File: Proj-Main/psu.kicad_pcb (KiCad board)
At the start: 2 copper layers, 100 x 75 mm, 129 parts, among them J1 T1A, J2 T1B, J3 T1C, J4 OUT+, J5 SENSE, J6 METER, J7 OUT-, Q1 BC856, Q10 PMP4201Y, Q11 MMBT3904, Q12 PMP4201Y, Q13 BC856, Q14 MMBT2907A, Q15 BC856, Q16 MMBT3904, Q17 BC856, Q18 MMBT3904, Q19 MMBT2907A, Q2 MMBT3904, Q20 MMBT3904, Q21 TIP105, Q22 PZT2222A, Q23 PMP4201Y, Q24 MMBT2907A, Q3 PZT2222A, Q4 BC856, Q5 PMP4201Y, Q6 MMBT3906, Q7 MMBT3906, Q8 PMP4201Y, Q9 MMBT3904

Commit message: PCB tweaks
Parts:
- moved Q2 7.00 mm to (138.0, 116.0), turned to 90 degrees
- moved R3 6.58 mm to (138.0, 122.0), turned to 180 degrees
- moved RV2 6.37 mm to (146.2, 103.2), turned to 0 degrees
- moved R2 5.32 mm to (138.0, 119.5), turned to 0 degrees
- moved R10 4.59 mm to (137.2, 105.0), turned to 270 degrees
- moved C10 4.53 mm to (164.0, 124.0)
- moved R48 4.53 mm to (167.0, 124.0)
- moved DZ1 4.51 mm to (141.5, 105.2)
- moved C1 4.50 mm to (133.5, 117.0)
- moved R1 4.50 mm to (133.5, 119.5)
- moved R4 4.50 mm to (133.5, 114.5)
- moved D9 3.78 mm to (141.5, 101.2), turned to 270 degrees
- moved C7 2.80 mm to (141.5, 94.8), turned to 0 degrees
- moved R15 1.52 mm to (141.0, 92.2), turned to 0 degrees
- moved TP4 1.41 mm to (137.5, 101.0)
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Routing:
- net CGND: track 428.0 -> 440.2 mm, vias 29 -> 28
- net Net-(C7-Pad2): track 18.2 -> 8.43 mm
- net Net-(DZ1-Pad1): track 29.2 -> 20.8 mm
- net GND: track 365.0 -> 372.4 mm, vias 22 -> 21
- net V-UNREG: track 243.2 -> 249.4 mm
- net Net-(Q1-Pad1): track 11.0 -> 4.86 mm
- net -12: track 279.4 -> 285.5 mm
- net Net-(RV1-Pad3): track 2.53 -> 8.54 mm
- net /OUT-: track 138.2 -> 132.4 mm
- net Net-(C1-Pad1): track 10.9 -> 5.58 mm
- net Net-(C1-Pad2): track 17.2 -> 12.0 mm
- net Net-(Q2-Pad1): track 7.07 -> 12.2 mm
- net Net-(C6-Pad2): track 5.20 -> 8.74 mm
- net +2: track 273.9 -> 271.1 mm, vias 10 -> 9
- net Net-(C11-Pad2): track 62.6 -> 60.0 mm
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
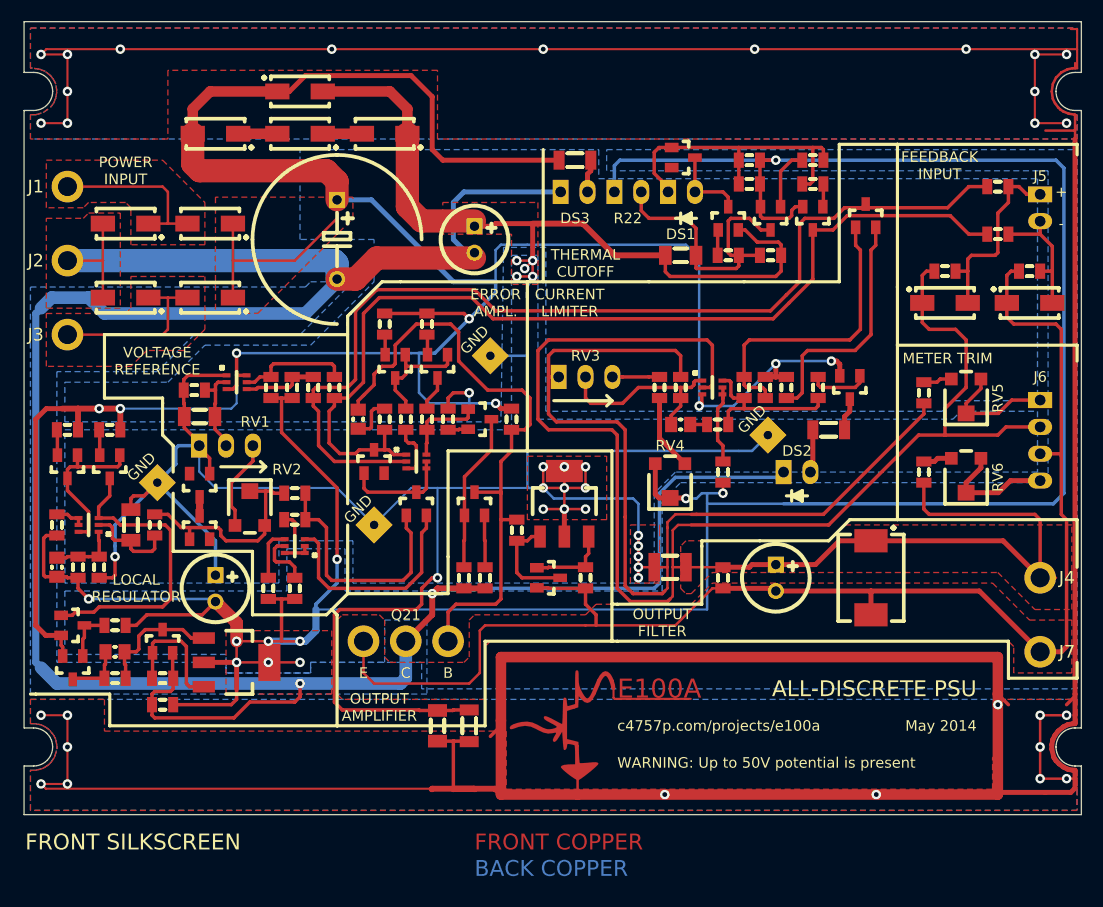
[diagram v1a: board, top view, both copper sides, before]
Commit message: Added guard traces, fixed overlapping components
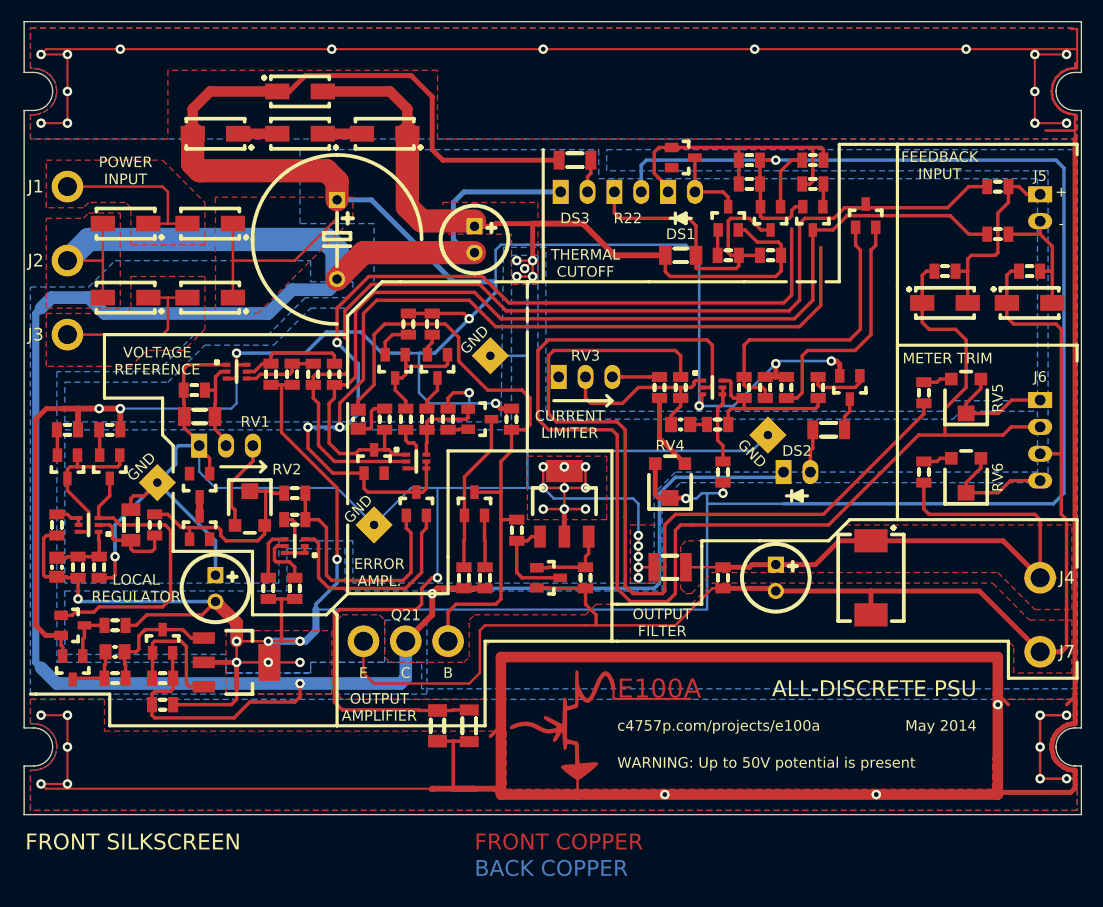
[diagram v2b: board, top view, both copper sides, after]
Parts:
- C1, C12: value 330p -> 1n
- DZ1: value BZX84B6V2 -> 6v2
- moved R23 2.25 mm to (161.2, 86.0)
- moved R16 1.25 mm to (148.2, 90.8)
- moved R17 1.25 mm to (150.2, 90.8)
- moved R18 1.25 mm to (152.2, 90.8)
- moved R19 1.25 mm to (154.2, 90.8)
- moved Q10 1.00 mm to (145.0, 90.5)
- moved R29 0.50 mm to (163.5, 86.0)
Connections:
- net Net-(D10-Pad1) renamed /GUARD
- R22 pad 1: -12 -> Net-(C8-Pad2)
- R22 pad 2: Net-(C8-Pad2) -> -12
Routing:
- net /GUARD: track 10.8 -> 149.8 mm, vias 0 -> 3
- net V-UNREG: track 249.4 -> 252.3 mm
- net Net-(C8-Pad2): track 27.3 -> 30.1 mm
- net /FB-: track 92.2 -> 94.4 mm
- net /FB+: track 95.9 -> 98.0 mm
- net Net-(Q13-Pad2): track 1.92 -> 3.69 mm
- net +2: track 271.1 -> 269.7 mm
- net /OUT+: track 180.6 -> 179.2 mm
- net Net-(C11-Pad2): track 60.0 -> 60.8 mm
- net Net-(C7-Pad2): track 8.43 -> 9.28 mm
- net GND: track 372.4 -> 373.2 mm

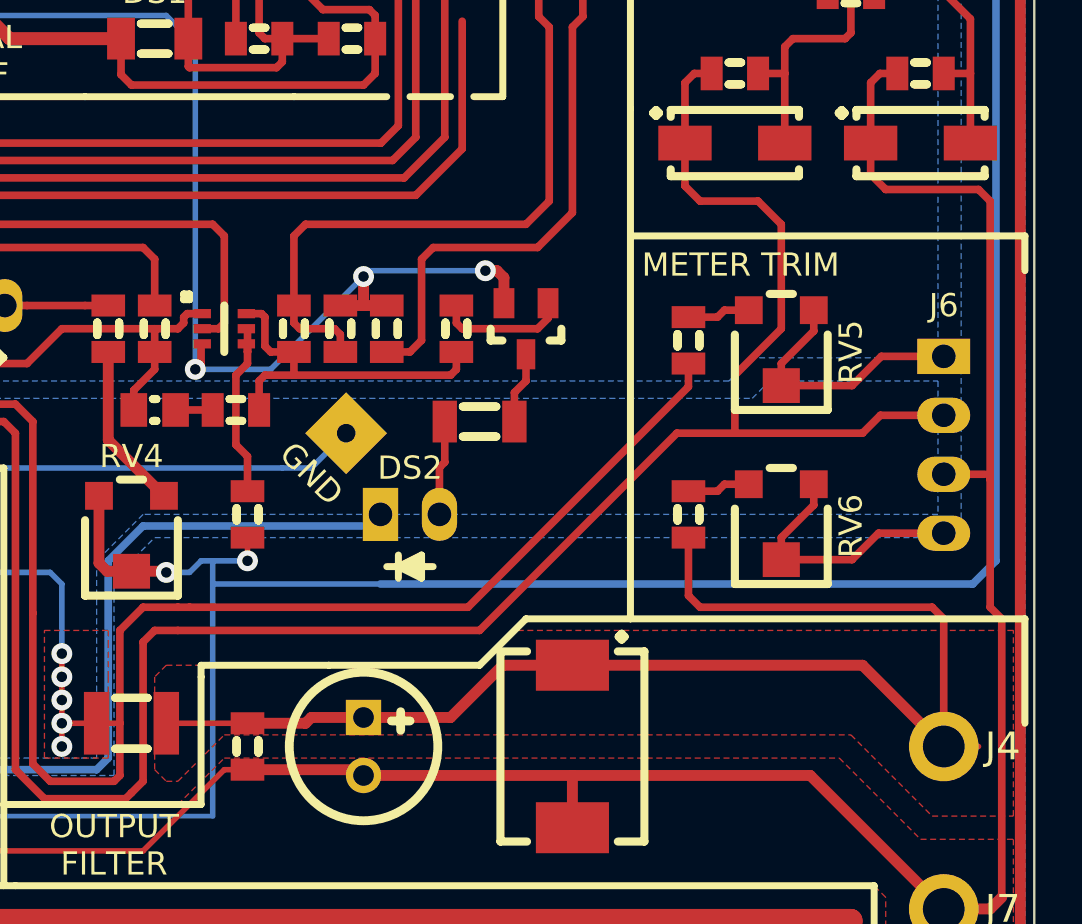
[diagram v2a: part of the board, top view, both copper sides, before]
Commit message: Corrected missing connection
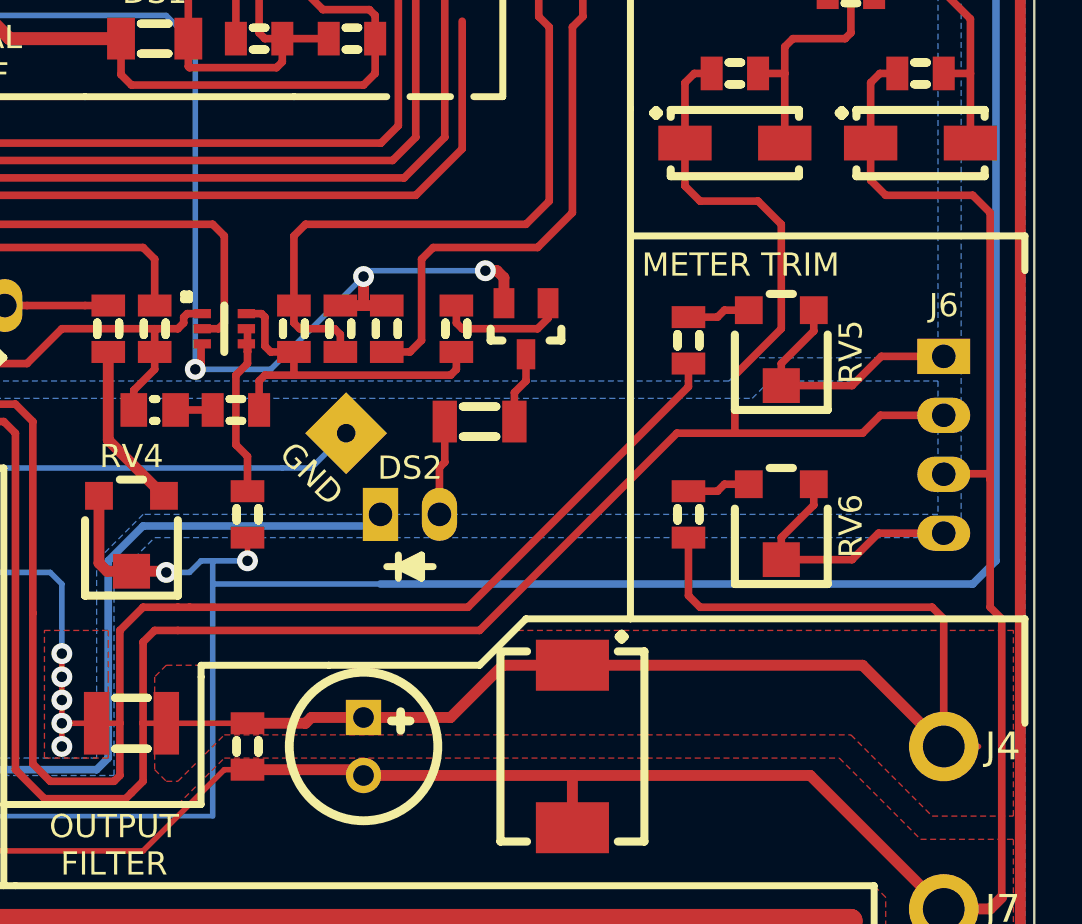
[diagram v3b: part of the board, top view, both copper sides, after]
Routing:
- net /OUT+: track 179.2 -> 180.2 mm
